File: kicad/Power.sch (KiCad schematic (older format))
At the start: 8 parts, among them P4 Battery, U5 LXDC2URxx

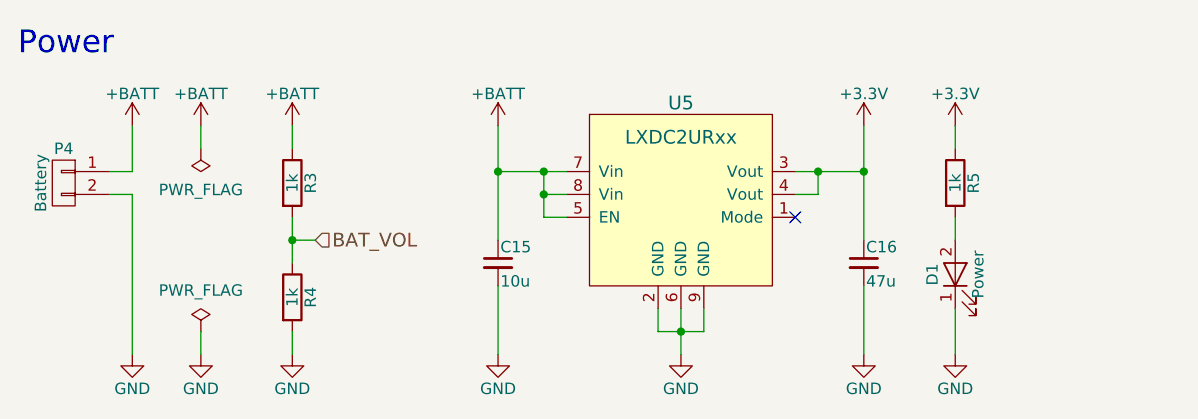
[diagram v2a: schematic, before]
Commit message: フットプリントを改良，アナログ電源を分離
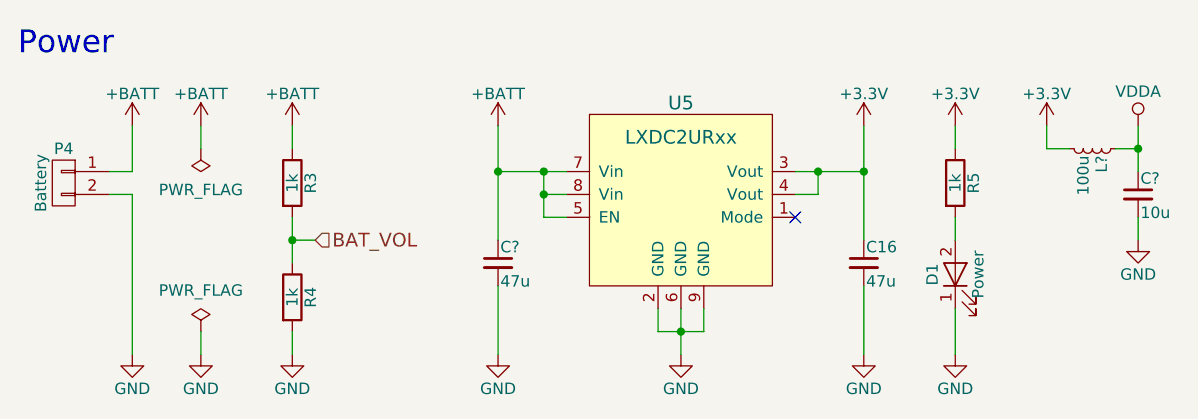
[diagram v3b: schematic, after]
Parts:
- removed C15: 10u, Capacitors_SMD:C_0603, symbol C_Small
- added C?: 10u, symbol C_Small
- added C?: 47u, Capacitors_SMD:C_0805, symbol C_Small
- added L?: 100u, symbol L_Small
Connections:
- net +3V3: now also L?.2
- net +BATT: now also C?.1
- net GND: now also C?.2, C?.2
- new net VDDA: C?.1, L?.1
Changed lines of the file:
@@
 	2000 4200 2000 4400
-$Comp
-L C_Small C15
-U 1 1 593DF9EE
-P 3600 4800
-F 0 "C15" H 3610 4870 50  0000 L CNN
-F 1 "10u" H 3610 4720 50  0000 L CNN
-F 2 "Capacitors_SMD:C_0603" H 3600 4800 50  0001 C CNN
-F 3 "" H 3600 4800 50  0000 C CNN
-	1    3600 4800
-	1    0    0    -1
-$EndComp
 $Comp
 L GND #PWR037
@@
 Wire Wire Line
 	5600 5000 5600 5200
+$Comp
+L +3.3V #PWR?
+U 1 1 59C37023
+P 6000 4200
+F 0 "#PWR?" H 6000 4050 50  0001 C CNN
+F 1 "+3.3V" H 6000 4340 50  0000 C CNN
+F 2 "" H 6000 4200 50  0001 C CNN
+F 3 "" H 6000 4200 50  0001 C CNN
+	1    6000 4200
+	1    0    0    -1
+$EndComp
+$Comp
+L VDDA #PWR?
+U 1 1 59C37047
+P 6400 4200
+F 0 "#PWR?" H 6400 4050 50  0001 C CNN
+F 1 "VDDA" H 6400 4350 50  0000 C CNN
+F 2 "" H 6400 4200 50  0001 C CNN
+F 3 "" H 6400 4200 50  0001 C CNN
+	1    6400 4200
+	1    0    0    -1
+$EndComp
+$Comp
+L L_Small L?
+U 1 1 59C3706B
+P 6200 4300
+F 0 "L?" H 6230 4340 50  0000 L CNN
+F 1 "100u" H 6230 4260 50  0000 L CNN
+F 2 "" H 6200 4300 50  0001 C CNN
+F 3 "" H 6200 4300 50  0001 C CNN
+	1    6200 4300
+	0    1    1    0
+$EndComp
+$Comp
+L C_Small C?
+U 1 1 59C370C1
+P 6400 4500
+F 0 "C?" H 6410 4570 50  0000 L CNN
+F 1 "10u" H 6410 4420 50  0000 L CNN
+F 2 "" H 6400 4500 50  0001 C CNN
+F 3 "" H 6400 4500 50  0001 C CNN
+	1    6400 4500
+	1    0    0    -1
+$EndComp
+Wire Wire Line
+	6400 4200 6400 4400
+$Comp
+L GND #PWR?
+U 1 1 59C37170
+P 6400 4700
+F 0 "#PWR?" H 6400 4450 50  0001 C CNN
+F 1 "GND" H 6400 4550 50  0000 C CNN
+F 2 "" H 6400 4700 50  0000 C CNN
+F 3 "" H 6400 4700 50  0000 C CNN
+	1    6400 4700
+	1    0    0    -1
+$EndComp
+Wire Wire Line
+	6400 4700 6400 4600
+Wire Wire Line
+	6300 4300 6400 4300
+Connection ~ 6400 4300
+Wire Wire Line
+	6100 4300 6000 4300
+Wire Wire Line
+	6000 4300 6000 4200
+$Comp
+L C_Small C?
+U 1 1 59C37F58
+P 3600 4800
+F 0 "C?" H 3610 4870 50  0000 L CNN
+F 1 "47u" H 3610 4720 50  0000 L CNN
+F 2 "Capacitors_SMD:C_0805" H 3600 4800 50  0001 C CNN
+F 3 "" H 3600 4800 50  0000 C CNN
+	1    3600 4800
+	1    0    0    -1
+$EndComp
 $EndSCHEMATC

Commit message: 回路とフットプリントを改良
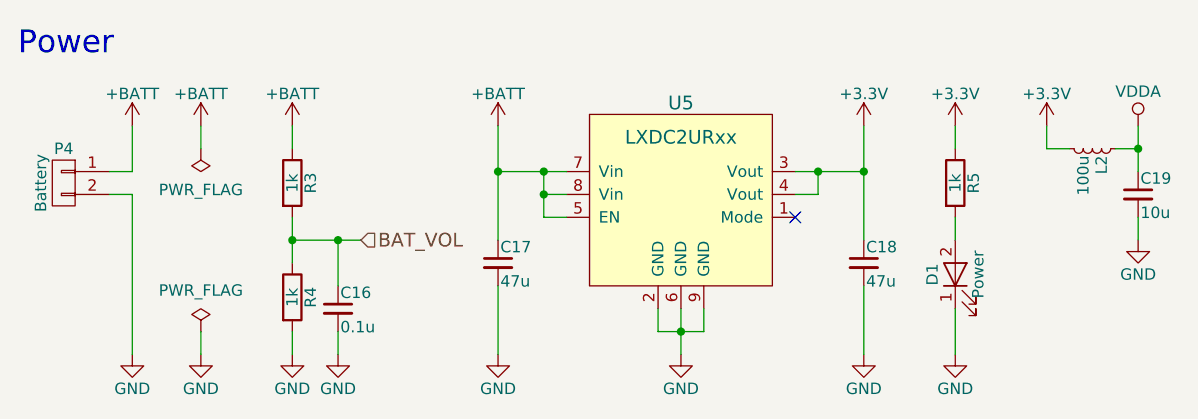
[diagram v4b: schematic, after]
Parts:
- added C16: 0.1u, Capacitors_SMD:C_0201, symbol C_Small
- C19: renamed from C?; footprint (none) -> Capacitors_SMD:C_0402
- L2: renamed from L?; footprint (none) -> Capacitors_SMD:C_0603
- gave numbers to parts that had none: 1
- renumbered C16 to C18
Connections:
- net BAT_VOL: now also C16.1
- net GND: now also C16.2
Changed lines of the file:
@@
 $EndDescr
 $Comp
-L +BATT #PWR023
+L +BATT #PWR024
 U 1 1 57CC111A
 P 2000 4200
-F 0 "#PWR023" H 2000 4050 50  0001 C CNN
+F 0 "#PWR024" H 2000 4050 50  0001 C CNN
 F 1 "+BATT" H 2000 4340 50  0000 C CNN
 F 2 "" H 2000 4200 50  0000 C CNN
@@
 $EndComp
 $Comp
-L GND #PWR024
+L GND #PWR025
 U 1 1 57CD3C05
 P 2700 5200
-F 0 "#PWR024" H 2700 4950 50  0001 C CNN
+F 0 "#PWR025" H 2700 4950 50  0001 C CNN
 F 1 "GND" H 2700 5050 50  0000 C CNN
 F 2 "" H 2700 5200 50  0000 C CNN
@@
 	1    0    0    -1
 $EndComp
-Text HLabel 2800 4700 2    60   Input ~ 0
+Text HLabel 3000 4700 2    60   Input ~ 0
 BAT_VOL
 $Comp
-L GND #PWR025
+L GND #PWR026
 U 1 1 57D18DB8
 P 2300 5200
-F 0 "#PWR025" H 2300 4950 50  0001 C CNN
+F 0 "#PWR026" H 2300 4950 50  0001 C CNN
 F 1 "GND" H 2300 5050 50  0000 C CNN
 F 2 "" H 2300 5200 50  0000 C CNN
@@
 $EndComp
 $Comp
-L PWR_FLAG #FLG026
+L PWR_FLAG #FLG027
 U 1 1 57D18DE7
 P 2300 5100
-F 0 "#FLG026" H 2300 5195 50  0001 C CNN
+F 0 "#FLG027" H 2300 5195 50  0001 C CNN
 F 1 "PWR_FLAG" H 2300 5280 50  0000 C CNN
 F 2 "" H 2300 5100 50  0000 C CNN
@@
 $EndComp
 $Comp
-L PWR_FLAG #FLG027
+L PWR_FLAG #FLG028
 U 1 1 57D1915C
 P 2300 4300
-F 0 "#FLG027" H 2300 4395 50  0001 C CNN
+F 0 "#FLG028" H 2300 4395 50  0001 C CNN
 F 1 "PWR_FLAG" H 2300 4480 50  0000 C CNN
 F 2 "" H 2300 4300 50  0000 C CNN
@@
 $EndComp
 $Comp
-L +BATT #PWR028
+L +BATT #PWR029
 U 1 1 57D1923B
 P 2300 4200
-F 0 "#PWR028" H 2300 4050 50  0001 C CNN
+F 0 "#PWR029" H 2300 4050 50  0001 C CNN
 F 1 "+BATT" H 2300 4340 50  0000 C CNN
 F 2 "" H 2300 4200 50  0000 C CNN
@@
 $EndComp
 $Comp
-L GND #PWR029
+L GND #PWR030
 U 1 1 57D00A42
 P 5600 5200
-F 0 "#PWR029" H 5600 4950 50  0001 C CNN
+F 0 "#PWR030" H 5600 4950 50  0001 C CNN
 F 1 "GND" H 5600 5050 50  0000 C CNN
 F 2 "" H 5600 5200 50  0000 C CNN
@@
 $EndComp
 $Comp
-L +BATT #PWR030
+L +BATT #PWR031
 U 1 1 57CD3CA2
 P 2700 4200
-F 0 "#PWR030" H 2700 4050 50  0001 C CNN
+F 0 "#PWR031" H 2700 4050 50  0001 C CNN
 F 1 "+BATT" H 2700 4340 50  0000 C CNN
 F 2 "" H 2700 4200 50  0000 C CNN
@@
 $EndComp
 $Comp
-L +3.3V #PWR031
+L +3.3V #PWR032
 U 1 1 589CB64F
 P 5600 4200
-F 0 "#PWR031" H 5600 4050 50  0001 C CNN
+F 0 "#PWR032" H 5600 4050 50  0001 C CNN
 F 1 "+3.3V" H 5600 4340 50  0000 C CNN
 F 2 "" H 5600 4200 50  0000 C CNN
@@
 $EndComp
 $Comp
-L +BATT #PWR032
+L +BATT #PWR033
 U 1 1 592A5000
 P 3600 4200
-F 0 "#PWR032" H 3600 4050 50  0001 C CNN
+F 0 "#PWR033" H 3600 4050 50  0001 C CNN
 F 1 "+BATT" H 3600 4340 50  0000 C CNN
 F 2 "" H 3600 4200 50  0000 C CNN
@@
 $EndComp
 $Comp
-L GND #PWR033
+L GND #PWR034
 U 1 1 592A5376
 P 4400 5200
-F 0 "#PWR033" H 4400 4950 50  0001 C CNN
+F 0 "#PWR034" H 4400 4950 50  0001 C CNN
 F 1 "GND" H 4400 5050 50  0000 C CNN
 F 2 "" H 4400 5200 50  0000 C CNN
@@
 $EndComp
 $Comp
-L +3.3V #PWR034
+L +3.3V #PWR035
 U 1 1 592A5664
 P 5200 4200
-F 0 "#PWR034" H 5200 4050 50  0001 C CNN
+F 0 "#PWR035" H 5200 4050 50  0001 C CNN
 F 1 "+3.3V" H 5200 4340 50  0000 C CNN
 F 2 "" H 5200 4200 50  0000 C CNN
@@
 NoConn ~ 4900 4600
 $Comp
-L C_Small C16
+L C_Small C18
 U 1 1 592A5C4A
 P 5200 4800
-F 0 "C16" H 5210 4870 50  0000 L CNN
+F 0 "C18" H 5210 4870 50  0000 L CNN
 F 1 "47u" H 5210 4720 50  0000 L CNN
 F 2 "Capacitors_SMD:C_0805" H 5200 4800 50  0001 C CNN
@@
 $EndComp
 $Comp
-L GND #PWR035
+L GND #PWR036
 U 1 1 592A5C9B
 P 5200 5200
-F 0 "#PWR035" H 5200 4950 50  0001 C CNN
+F 0 "#PWR036" H 5200 4950 50  0001 C CNN
 F 1 "GND" H 5200 5050 50  0000 C CNN
 F 2 "" H 5200 5200 50  0000 C CNN
@@
 $EndComp
 $Comp
-L GND #PWR036
+L GND #PWR037
 U 1 1 57CC113A
 P 2000 5200
-F 0 "#PWR036" H 2000 4950 50  0001 C CNN
+F 0 "#PWR037" H 2000 4950 50  0001 C CNN
 F 1 "GND" H 2000 5050 50  0000 C CNN
 F 2 "" H 2000 5200 50  0000 C CNN
@@
 	2700 4200 2700 4300
 Wire Wire Line
-	2800 4700 2700 4700
+	2700 4700 3000 4700
 Wire Wire Line
 	2700 4600 2700 4800
@@
 	2000 4200 2000 4400
 $Comp
-L GND #PWR037
+L GND #PWR038
 U 1 1 593DFA5D
 P 3600 5200
-F 0 "#PWR037" H 3600 4950 50  0001 C CNN
+F 0 "#PWR038" H 3600 4950 50  0001 C CNN
 F 1 "GND" H 3600 5050 50  0000 C CNN
 F 2 "" H 3600 5200 50  0000 C CNN
@@
 	5600 5000 5600 5200
 $Comp
-L +3.3V #PWR?
+L +3.3V #PWR039
 U 1 1 59C37023
 P 6000 4200
-F 0 "#PWR?" H 6000 4050 50  0001 C CNN
+F 0 "#PWR039" H 6000 4050 50  0001 C CNN
 F 1 "+3.3V" H 6000 4340 50  0000 C CNN
 F 2 "" H 6000 4200 50  0001 C CNN
@@
 $EndComp
 $Comp
-L VDDA #PWR?
+L VDDA #PWR040
 U 1 1 59C37047
 P 6400 4200
-F 0 "#PWR?" H 6400 4050 50  0001 C CNN
+F 0 "#PWR040" H 6400 4050 50  0001 C CNN
 F 1 "VDDA" H 6400 4350 50  0000 C CNN
 F 2 "" H 6400 4200 50  0001 C CNN
@@
 $EndComp
 $Comp
-L L_Small L?
+L L_Small L2
 U 1 1 59C3706B
 P 6200 4300
-F 0 "L?" H 6230 4340 50  0000 L CNN
+F 0 "L2" H 6230 4340 50  0000 L CNN
 F 1 "100u" H 6230 4260 50  0000 L CNN
-F 2 "" H 6200 4300 50  0001 C CNN
+F 2 "Capacitors_SMD:C_0603" H 6200 4300 50  0001 C CNN
 F 3 "" H 6200 4300 50  0001 C CNN
 	1    6200 4300
@@
 $EndComp
 $Comp
-L C_Small C?
+L C_Small C19
 U 1 1 59C370C1
 P 6400 4500
-F 0 "C?" H 6410 4570 50  0000 L CNN
+F 0 "C19" H 6410 4570 50  0000 L CNN
 F 1 "10u" H 6410 4420 50  0000 L CNN
-F 2 "" H 6400 4500 50  0001 C CNN
+F 2 "Capacitors_SMD:C_0402" H 6400 4500 50  0001 C CNN
 F 3 "" H 6400 4500 50  0001 C CNN
 	1    6400 4500
@@
 	6400 4200 6400 4400
 $Comp
-L GND #PWR?
+L GND #PWR041
 U 1 1 59C37170
 P 6400 4700
-F 0 "#PWR?" H 6400 4450 50  0001 C CNN
+F 0 "#PWR041" H 6400 4450 50  0001 C CNN
 F 1 "GND" H 6400 4550 50  0000 C CNN
 F 2 "" H 6400 4700 50  0000 C CNN
@@
 	6000 4300 6000 4200
 $Comp
-L C_Small C?
+L C_Small C17
 U 1 1 59C37F58
 P 3600 4800
-F 0 "C?" H 3610 4870 50  0000 L CNN
+F 0 "C17" H 3610 4870 50  0000 L CNN
 F 1 "47u" H 3610 4720 50  0000 L CNN
 F 2 "Capacitors_SMD:C_0805" H 3600 4800 50  0001 C CNN
@@
 	1    0    0    -1
 $EndComp
+$Comp
+L C_Small C16
+U 1 1 59C47577
+P 2900 5000
+F 0 "C16" H 2910 5070 50  0000 L CNN
+F 1 "0.1u" H 2910 4920 50  0000 L CNN
+F 2 "Capacitors_SMD:C_0201" H 2900 5000 50  0001 C CNN
+F 3 "" H 2900 5000 50  0001 C CNN
+	1    2900 5000
+	1    0    0    -1
+$EndComp
+$Comp
+L GND #PWR042
+U 1 1 59C475E6
+P 2900 5200
+F 0 "#PWR042" H 2900 4950 50  0001 C CNN
+F 1 "GND" H 2900 5050 50  0000 C CNN
+F 2 "" H 2900 5200 50  0000 C CNN
+F 3 "" H 2900 5200 50  0000 C CNN
+	1    2900 5200
+	1    0    0    -1
+$EndComp
+Wire Wire Line
+	2900 4700 2900 4900
+Connection ~ 2900 4700
+Wire Wire Line
+	2900 5100 2900 5200
 $EndSCHEMATC

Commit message: 自動配線1残し
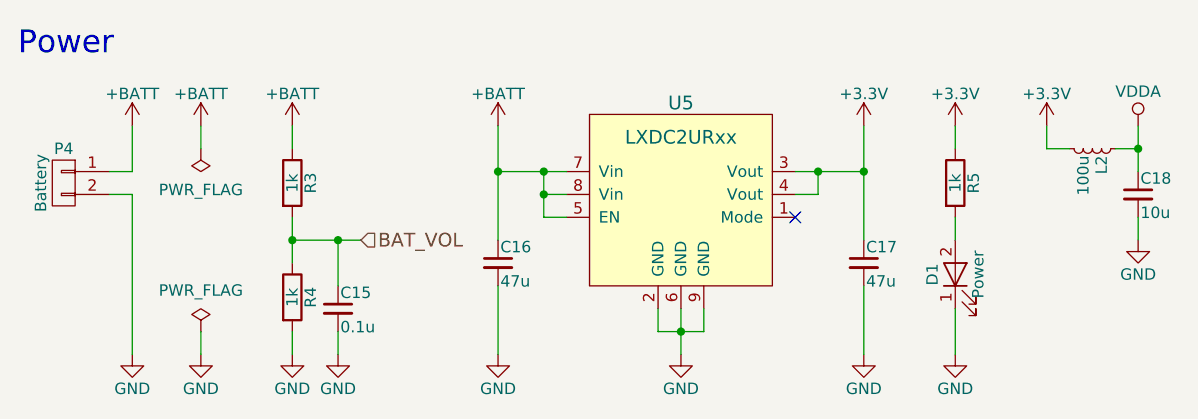
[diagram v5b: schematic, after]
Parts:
- renumbered C16 to C15, C17 to C16, C18 to C17, C19 to C18
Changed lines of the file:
@@
 NoConn ~ 4900 4600
 $Comp
-L C_Small C18
+L C_Small C17
 U 1 1 592A5C4A
 P 5200 4800
-F 0 "C18" H 5210 4870 50  0000 L CNN
+F 0 "C17" H 5210 4870 50  0000 L CNN
 F 1 "47u" H 5210 4720 50  0000 L CNN
 F 2 "Capacitors_SMD:C_0805" H 5200 4800 50  0001 C CNN
@@
 $EndComp
 $Comp
-L C_Small C19
+L C_Small C18
 U 1 1 59C370C1
 P 6400 4500
-F 0 "C19" H 6410 4570 50  0000 L CNN
+F 0 "C18" H 6410 4570 50  0000 L CNN
 F 1 "10u" H 6410 4420 50  0000 L CNN
 F 2 "Capacitors_SMD:C_0402" H 6400 4500 50  0001 C CNN
@@
 	6000 4300 6000 4200
 $Comp
-L C_Small C17
+L C_Small C16
 U 1 1 59C37F58
 P 3600 4800
-F 0 "C17" H 3610 4870 50  0000 L CNN
+F 0 "C16" H 3610 4870 50  0000 L CNN
 F 1 "47u" H 3610 4720 50  0000 L CNN
 F 2 "Capacitors_SMD:C_0805" H 3600 4800 50  0001 C CNN
@@
 $EndComp
 $Comp
-L C_Small C16
+L C_Small C15
 U 1 1 59C47577
 P 2900 5000
-F 0 "C16" H 2910 5070 50  0000 L CNN
+F 0 "C15" H 2910 5070 50  0000 L CNN
 F 1 "0.1u" H 2910 4920 50  0000 L CNN
 F 2 "Capacitors_SMD:C_0201" H 2900 5000 50  0001 C CNN

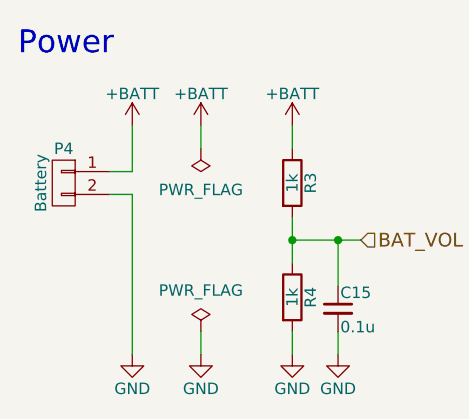
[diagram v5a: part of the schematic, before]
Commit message: 実装経験をもとにフットプリントを改良，ミスを修正
SC70サイズのオペアンプのピンアサインを修正
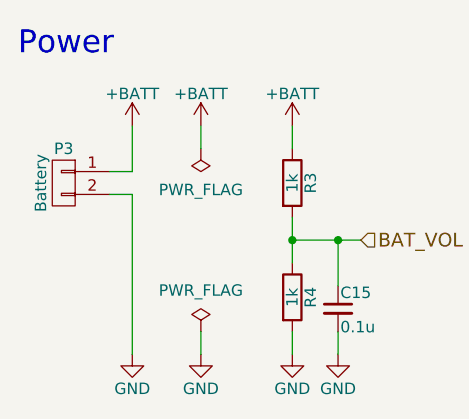
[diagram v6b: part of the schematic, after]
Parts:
- renumbered P4 to P3
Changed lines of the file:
@@
 $EndDescr
 $Comp
-L +BATT #PWR024
+L +BATT #PWR24
 U 1 1 57CC111A
 P 2000 4200
-F 0 "#PWR024" H 2000 4050 50  0001 C CNN
+F 0 "#PWR24" H 2000 4050 50  0001 C CNN
 F 1 "+BATT" H 2000 4340 50  0000 C CNN
 F 2 "" H 2000 4200 50  0000 C CNN
@@
 $EndComp
 $Comp
-L GND #PWR025
+L GND #PWR29
 U 1 1 57CD3C05
 P 2700 5200
-F 0 "#PWR025" H 2700 4950 50  0001 C CNN
+F 0 "#PWR29" H 2700 4950 50  0001 C CNN
 F 1 "GND" H 2700 5050 50  0000 C CNN
 F 2 "" H 2700 5200 50  0000 C CNN
@@
 BAT_VOL
 $Comp
-L GND #PWR026
+L GND #PWR27
 U 1 1 57D18DB8
 P 2300 5200
-F 0 "#PWR026" H 2300 4950 50  0001 C CNN
+F 0 "#PWR27" H 2300 4950 50  0001 C CNN
 F 1 "GND" H 2300 5050 50  0000 C CNN
 F 2 "" H 2300 5200 50  0000 C CNN
@@
 $EndComp
 $Comp
-L PWR_FLAG #FLG027
+L PWR_FLAG #FLG2
 U 1 1 57D18DE7
 P 2300 5100
-F 0 "#FLG027" H 2300 5195 50  0001 C CNN
+F 0 "#FLG2" H 2300 5195 50  0001 C CNN
 F 1 "PWR_FLAG" H 2300 5280 50  0000 C CNN
 F 2 "" H 2300 5100 50  0000 C CNN
@@
 $EndComp
 $Comp
-L PWR_FLAG #FLG028
+L PWR_FLAG #FLG1
 U 1 1 57D1915C
 P 2300 4300
-F 0 "#FLG028" H 2300 4395 50  0001 C CNN
+F 0 "#FLG1" H 2300 4395 50  0001 C CNN
 F 1 "PWR_FLAG" H 2300 4480 50  0000 C CNN
 F 2 "" H 2300 4300 50  0000 C CNN
@@
 $EndComp
 $Comp
-L +BATT #PWR029
+L +BATT #PWR26
 U 1 1 57D1923B
 P 2300 4200
-F 0 "#PWR029" H 2300 4050 50  0001 C CNN
+F 0 "#PWR26" H 2300 4050 50  0001 C CNN
 F 1 "+BATT" H 2300 4340 50  0000 C CNN
 F 2 "" H 2300 4200 50  0000 C CNN
@@
 $EndComp
 $Comp
-L GND #PWR030
+L GND #PWR37
 U 1 1 57D00A42
 P 5600 5200
-F 0 "#PWR030" H 5600 4950 50  0001 C CNN
+F 0 "#PWR37" H 5600 4950 50  0001 C CNN
 F 1 "GND" H 5600 5050 50  0000 C CNN
 F 2 "" H 5600 5200 50  0000 C CNN
@@
 $EndComp
 $Comp
-L CONN_01X02 P4
+L CONN_01X02 P3
 U 1 1 57D07AC8
 P 1700 4450
-F 0 "P4" H 1700 4600 50  0000 C CNN
+F 0 "P3" H 1700 4600 50  0000 C CNN
 F 1 "Battery" V 1800 4450 50  0000 C CNN
 F 2 "Connectors_Hirose:Hirose_DF13-02P-1.25DSA_02x1.25mm_Straight" H 1700 4450 50  0001 C CNN
@@
 $EndComp
 $Comp
-L +BATT #PWR031
+L +BATT #PWR28
 U 1 1 57CD3CA2
 P 2700 4200
-F 0 "#PWR031" H 2700 4050 50  0001 C CNN
+F 0 "#PWR28" H 2700 4050 50  0001 C CNN
 F 1 "+BATT" H 2700 4340 50  0000 C CNN
 F 2 "" H 2700 4200 50  0000 C CNN
@@
 $EndComp
 $Comp
-L +3.3V #PWR032
+L +3.3V #PWR36
 U 1 1 589CB64F
 P 5600 4200
-F 0 "#PWR032" H 5600 4050 50  0001 C CNN
+F 0 "#PWR36" H 5600 4050 50  0001 C CNN
 F 1 "+3.3V" H 5600 4340 50  0000 C CNN
 F 2 "" H 5600 4200 50  0000 C CNN
@@
 $EndComp
 $Comp
-L +BATT #PWR033
+L +BATT #PWR31
 U 1 1 592A5000
 P 3600 4200
-F 0 "#PWR033" H 3600 4050 50  0001 C CNN
+F 0 "#PWR31" H 3600 4050 50  0001 C CNN
 F 1 "+BATT" H 3600 4340 50  0000 C CNN
 F 2 "" H 3600 4200 50  0000 C CNN
@@
 $EndComp
 $Comp
-L GND #PWR034
+L GND #PWR33
 U 1 1 592A5376
 P 4400 5200
-F 0 "#PWR034" H 4400 4950 50  0001 C CNN
+F 0 "#PWR33" H 4400 4950 50  0001 C CNN
 F 1 "GND" H 4400 5050 50  0000 C CNN
 F 2 "" H 4400 5200 50  0000 C CNN
@@
 $EndComp
 $Comp
-L +3.3V #PWR035
+L +3.3V #PWR34
 U 1 1 592A5664
 P 5200 4200
-F 0 "#PWR035" H 5200 4050 50  0001 C CNN
+F 0 "#PWR34" H 5200 4050 50  0001 C CNN
 F 1 "+3.3V" H 5200 4340 50  0000 C CNN
 F 2 "" H 5200 4200 50  0000 C CNN
@@
 $EndComp
 $Comp
-L GND #PWR036
+L GND #PWR35
 U 1 1 592A5C9B
 P 5200 5200
-F 0 "#PWR036" H 5200 4950 50  0001 C CNN
+F 0 "#PWR35" H 5200 4950 50  0001 C CNN
 F 1 "GND" H 5200 5050 50  0000 C CNN
 F 2 "" H 5200 5200 50  0000 C CNN
@@
 $EndComp
 $Comp
-L GND #PWR037
+L GND #PWR25
 U 1 1 57CC113A
 P 2000 5200
-F 0 "#PWR037" H 2000 4950 50  0001 C CNN
+F 0 "#PWR25" H 2000 4950 50  0001 C CNN
 F 1 "GND" H 2000 5050 50  0000 C CNN
 F 2 "" H 2000 5200 50  0000 C CNN
@@
 	2000 4200 2000 4400
 $Comp
-L GND #PWR038
+L GND #PWR32
 U 1 1 593DFA5D
 P 3600 5200
-F 0 "#PWR038" H 3600 4950 50  0001 C CNN
+F 0 "#PWR32" H 3600 4950 50  0001 C CNN
 F 1 "GND" H 3600 5050 50  0000 C CNN
 F 2 "" H 3600 5200 50  0000 C CNN
@@
 	5600 5000 5600 5200
 $Comp
-L +3.3V #PWR039
+L +3.3V #PWR38
 U 1 1 59C37023
 P 6000 4200
-F 0 "#PWR039" H 6000 4050 50  0001 C CNN
+F 0 "#PWR38" H 6000 4050 50  0001 C CNN
 F 1 "+3.3V" H 6000 4340 50  0000 C CNN
 F 2 "" H 6000 4200 50  0001 C CNN
@@
 $EndComp
 $Comp
-L VDDA #PWR040
+L VDDA #PWR39
 U 1 1 59C37047
 P 6400 4200
-F 0 "#PWR040" H 6400 4050 50  0001 C CNN
+F 0 "#PWR39" H 6400 4050 50  0001 C CNN
 F 1 "VDDA" H 6400 4350 50  0000 C CNN
 F 2 "" H 6400 4200 50  0001 C CNN
@@
 	6400 4200 6400 4400
 $Comp
-L GND #PWR041
+L GND #PWR40
 U 1 1 59C37170
 P 6400 4700
-F 0 "#PWR041" H 6400 4450 50  0001 C CNN
+F 0 "#PWR40" H 6400 4450 50  0001 C CNN
 F 1 "GND" H 6400 4550 50  0000 C CNN
 F 2 "" H 6400 4700 50  0000 C CNN
@@
 $EndComp
 $Comp
-L GND #PWR042
+L GND #PWR30
 U 1 1 59C475E6
 P 2900 5200
-F 0 "#PWR042" H 2900 4950 50  0001 C CNN
+F 0 "#PWR30" H 2900 4950 50  0001 C CNN
 F 1 "GND" H 2900 5050 50  0000 C CNN
 F 2 "" H 2900 5200 50  0000 C CNN
